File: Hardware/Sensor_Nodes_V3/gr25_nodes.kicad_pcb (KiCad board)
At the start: 4 copper layers, 22.4 x 70.5 mm, 74 parts, among them J1 Conn_01x06_Socket, J2 Conn_01x27_Socket, J3 Conn_01x27_Socket, Q1 S9013, U1 STM32F103C8Tx, U2 STM32G474RBTx, U3 MCP2542FDxMF, U4 MCP2542FDxMF, U5 AMS1117-3.3, U6 TPS563200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

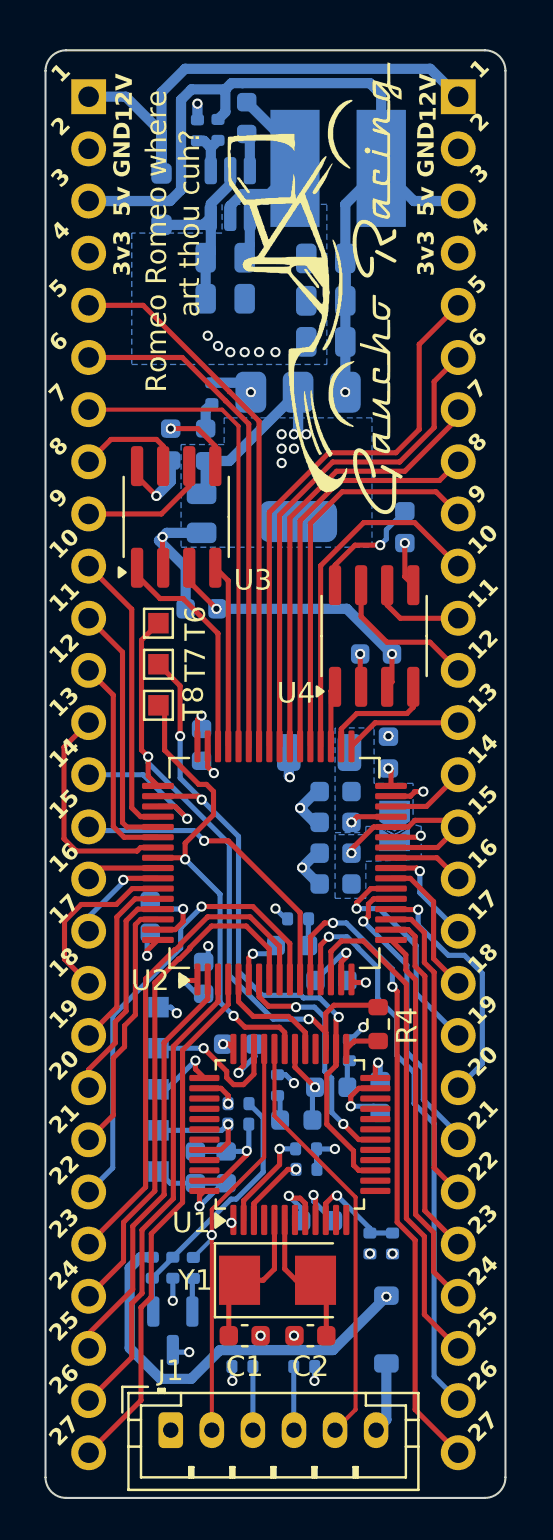
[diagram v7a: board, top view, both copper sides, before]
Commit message: added a neopixel and moved some pins around
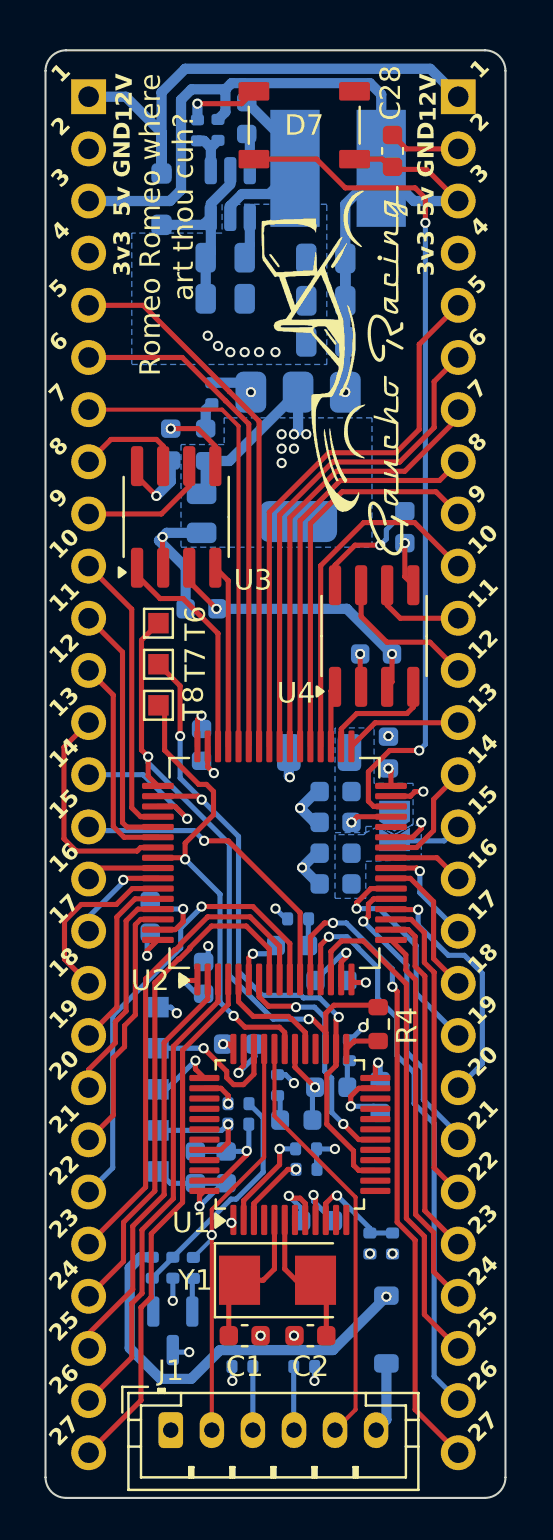
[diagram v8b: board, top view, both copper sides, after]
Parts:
- removed the G*** at (121.7, 39.1)
- added C28: 100nF, Capacitor_SMD:C_0603_1608Metric, F.Cu at (125.5, 32.4)
- added D7: WS2812B, LED_SMD:LED_WS2812B_PLCC4_5.0x5.0mm_P3.2mm, F.Cu at (121.2, 31.2)
- added G***: LOGO, LOGO:grloho, F.Cu at (119.4, 43.1)
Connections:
- C16 pad 1: PB2/VREF -> VREF
- C19 pad 1: PB2/VREF -> VREF
- J2 pad 14: PB10 -> PB2
- J2 pad 15: PB2/VREF -> VREF
- JP1 pad 2: PB2/VREF -> VREF
- U2 pad 26: PB2/VREF -> PB2
- U2 pad 28: PB2/VREF -> VREF
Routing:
- net PB10: track 3.91 -> 41.3 mm, vias 0 -> 2
- net PB2/VREF: track 9.80 -> 0.00 mm, vias 1 -> 0
- net GND: track 65.5 -> 72.3 mm
- net +5V: track 122.7 -> 128.6 mm
- net PB2: track 0.00 -> 5.63 mm
- net VREF: track 0.00 -> 3.38 mm
- added copper zone on B.Cu, net VREF
- removed copper zone on B.Cu, net PB2/VREF
